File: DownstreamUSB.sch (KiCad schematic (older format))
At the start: 2 parts, among them J4 USB_A

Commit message: Replace 100 uF caps
The ones I had selected before were only rated for 4V, and I need at least 5V (USB bus).
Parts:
- C17: Manufacturer_Part_Number TPST107M004R0500 -> TACT107M006XTA; Price 0.93 -> 4.4; Vendor Part Number 581-TPST107M004R0500 -> 581-TACT107M006XTA
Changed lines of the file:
@@
 F 1 "100μF" H 5435 3055 50 0000 R CNN
 F 2 "Capacitor_SMD:C_1210_3225Metric" H 5588 2950 50 0001 C CNN
-F 3 "https://www.mouser.com/datasheet/2/40/TPS-2066671.pdf" H 5550 3100 50 0001 C CNN
+F 3 "https://www.mouser.com/datasheet/2/40/tac-776418.pdf" H 5550 3100 50 0001 C CNN
 F 4 "AVX" H 5435 3246 50 0001 C CNN "Manufacturer_Name"
-F 5 "TPST107M004R0500" H 5435 3246 50 0001 C CNN "Manufacturer_Part_Number"
-F 6 "0.93" H 5435 3246 50 0001 C CNN "Price"
-F 7 "581-TPST107M004R0500" H 5435 3246 50 0001 C CNN "Vendor Part Number"
+F 5 "TACT107M006XTA" H 5435 3246 50 0001 C CNN "Manufacturer_Part_Number"
+F 6 "4.4" H 5435 3246 50 0001 C CNN "Price"
+F 7 "581-TACT107M006XTA" H 5435 3246 50 0001 C CNN "Vendor Part Number"
 F 8 "Mouser" H 5435 3246 50 0001 C CNN "Vendor"
 	1    5550 3100

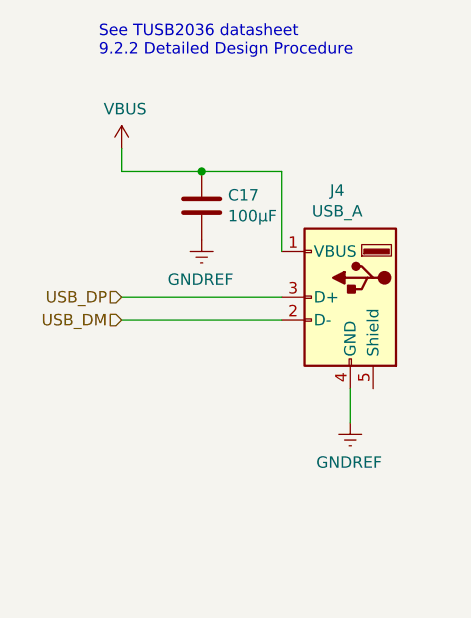
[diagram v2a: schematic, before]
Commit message: Add ID markings on schema and pcb
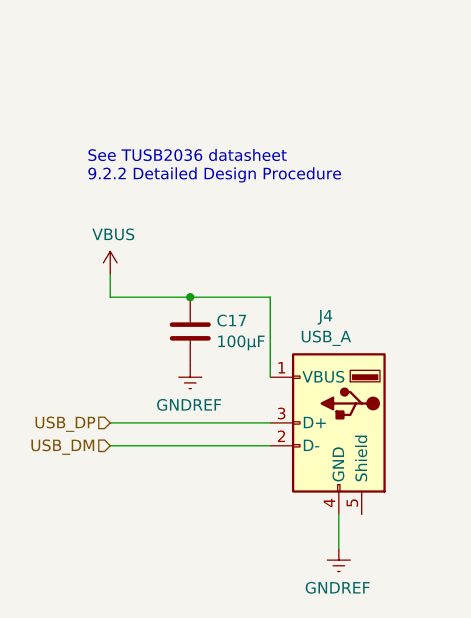
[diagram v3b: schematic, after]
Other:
- moved on the sheet: C17, J4
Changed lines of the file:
@@
 encoding utf-8
 Sheet 6 6
-Title ""
-Date ""
-Rev ""
-Comp ""
+Title "TX-500 Data Interface"
+Date "2021-03-15"
+Rev "0.1"
+Comp "Chris Keller K0SWE"
 Comment1 ""
 Comment2 ""
@@
 L power:GNDREF #PWR?
 U 1 1 6054D05F
-P 5550 3250
+P 5500 3800
 AR Path="/6057976E/6054D05F" Ref="#PWR?"  Part="1"
 AR Path="/605B3ED2/6054D05F" Ref="#PWR0134"  Part="1"
-F 0 "#PWR0134" H 5550 3000 50  0001 C CNN
-F 1 "GNDREF" H 5555 3077 50  0000 C CNN
-F 2 "" H 5550 3250 50  0001 C CNN
-F 3 "" H 5550 3250 50  0001 C CNN
-	1    5550 3250
+F 0 "#PWR0134" H 5500 3550 50  0001 C CNN
+F 1 "GNDREF" H 5505 3627 50  0000 C CNN
+F 2 "" H 5500 3800 50  0001 C CNN
+F 3 "" H 5500 3800 50  0001 C CNN
+	1    5500 3800
 	-1   0    0    -1
 $EndComp
@@
 L power:GNDREF #PWR?
 U 1 1 605EED26
-P 6200 4050
+P 6150 4600
 AR Path="/6057976E/605EED26" Ref="#PWR?"  Part="1"
 AR Path="/605B3ED2/605EED26" Ref="#PWR0116"  Part="1"
-F 0 "#PWR0116" H 6200 3800 50  0001 C CNN
-F 1 "GNDREF" H 6205 3877 50  0000 C CNN
-F 2 "" H 6200 4050 50  0001 C CNN
-F 3 "" H 6200 4050 50  0001 C CNN
-	1    6200 4050
+F 0 "#PWR0116" H 6150 4350 50  0001 C CNN
+F 1 "GNDREF" H 6155 4427 50  0000 C CNN
+F 2 "" H 6150 4600 50  0001 C CNN
+F 3 "" H 6150 4600 50  0001 C CNN
+	1    6150 4600
 	-1   0    0    -1
 $EndComp
@@
 L power:VBUS #PWR0113
 U 1 1 605E55CB
-P 5200 2850
-F 0 "#PWR0113" H 5200 2700 50  0001 C CNN
-F 1 "VBUS" H 5215 3023 50  0000 C CNN
-F 2 "" H 5200 2850 50  0001 C CNN
-F 3 "" H 5200 2850 50  0001 C CNN
-	1    5200 2850
+P 5150 3400
+F 0 "#PWR0113" H 5150 3250 50  0001 C CNN
+F 1 "VBUS" H 5165 3573 50  0000 C CNN
+F 2 "" H 5150 3400 50  0001 C CNN
+F 3 "" H 5150 3400 50  0001 C CNN
+	1    5150 3400
 	1    0    0    -1
 $EndComp
@@
 L Connector:USB_A J?
 U 1 1 605B68EE
-P 6200 3500
+P 6150 4050
 AR Path="/605B68EE" Ref="J?"  Part="1"
 AR Path="/605B3ED2/605B68EE" Ref="J4"  Part="1"
-F 0 "J4" H 6257 3967 50  0000 C CNN
-F 1 "USB_A" H 6257 3876 50  0000 C CNN
-F 2 "Connector_USB:USB_A_Molex_67643_Horizontal" H 6350 3450 50  0001 C CNN
-F 3 "https://www.mouser.com/datasheet/2/276/1/0676433910_IO_CONNECTORS-172273.pdf" H 6350 3450 50  0001 C CNN
-F 4 "Downstream USB socket" H 6257 4067 50  0001 C CNN "Description"
-F 5 "Molex" H 6257 4067 50  0001 C CNN "Manufacturer_Name"
-F 6 "67643-3910" H 6257 4067 50  0001 C CNN "Manufacturer_Part_Number"
-F 7 "1.64" H 6257 4067 50  0001 C CNN "Price"
-F 8 "538-67643-3910" H 6257 4067 50  0001 C CNN "Vendor Part Number"
-F 9 "Mouser" H 6257 4067 50  0001 C CNN "Vendor"
-	1    6200 3500
+F 0 "J4" H 6207 4517 50  0000 C CNN
+F 1 "USB_A" H 6207 4426 50  0000 C CNN
+F 2 "Connector_USB:USB_A_Molex_67643_Horizontal" H 6300 4000 50  0001 C CNN
+F 3 "https://www.mouser.com/datasheet/2/276/1/0676433910_IO_CONNECTORS-172273.pdf" H 6300 4000 50  0001 C CNN
+F 4 "Downstream USB socket" H 6207 4617 50  0001 C CNN "Description"
+F 5 "Molex" H 6207 4617 50  0001 C CNN "Manufacturer_Name"
+F 6 "67643-3910" H 6207 4617 50  0001 C CNN "Manufacturer_Part_Number"
+F 7 "1.64" H 6207 4617 50  0001 C CNN "Price"
+F 8 "538-67643-3910" H 6207 4617 50  0001 C CNN "Vendor Part Number"
+F 9 "Mouser" H 6207 4617 50  0001 C CNN "Vendor"
+	1    6150 4050
 	-1   0    0    -1
 $EndComp
@@
 L Device:C C?
 U 1 1 605EE4F2
-P 5550 3100
+P 5500 3650
 AR Path="/605EE4F2" Ref="C?"  Part="1"
 AR Path="/6057976E/605EE4F2" Ref="C?"  Part="1"
 AR Path="/605B3ED2/605EE4F2" Ref="C17"  Part="1"
-F 0 "C17" H 5435 3146 50  0000 R CNN
-F 1 "100μF" H 5435 3055 50  0000 R CNN
-F 2 "Capacitor_SMD:C_1210_3225Metric" H 5588 2950 50  0001 C CNN
-F 3 "https://www.mouser.com/datasheet/2/40/tac-776418.pdf" H 5550 3100 50  0001 C CNN
-F 4 "AVX" H 5435 3246 50  0001 C CNN "Manufacturer_Name"
-F 5 "TACT107M006XTA" H 5435 3246 50  0001 C CNN "Manufacturer_Part_Number"
-F 6 "4.4" H 5435 3246 50  0001 C CNN "Price"
-F 7 "581-TACT107M006XTA" H 5435 3246 50  0001 C CNN "Vendor Part Number"
-F 8 "Mouser" H 5435 3246 50  0001 C CNN "Vendor"
-	1    5550 3100
+F 0 "C17" H 5385 3696 50  0000 R CNN
+F 1 "100μF" H 5385 3605 50  0000 R CNN
+F 2 "Capacitor_SMD:C_1210_3225Metric" H 5538 3500 50  0001 C CNN
+F 3 "https://www.mouser.com/datasheet/2/40/tac-776418.pdf" H 5500 3650 50  0001 C CNN
+F 4 "AVX" H 5385 3796 50  0001 C CNN "Manufacturer_Name"
+F 5 "TACT107M006XTA" H 5385 3796 50  0001 C CNN "Manufacturer_Part_Number"
+F 6 "4.4" H 5385 3796 50  0001 C CNN "Price"
+F 7 "581-TACT107M006XTA" H 5385 3796 50  0001 C CNN "Vendor Part Number"
+F 8 "Mouser" H 5385 3796 50  0001 C CNN "Vendor"
+	1    5500 3650
 	-1   0    0    -1
 $EndComp
-Text Notes 5100 2450 0    50   ~ 0
+Text Notes 5050 3000 0    50   ~ 0
 See TUSB2036 datasheet\n9.2.2 Detailed Design Procedure
-Text HLabel 5200 3500 0    50   Input ~ 0
+Text HLabel 5150 4050 0    50   Input ~ 0
 USB_DP
-Text HLabel 5200 3600 0    50   Input ~ 0
+Text HLabel 5150 4150 0    50   Input ~ 0
 USB_DM
 Wire Wire Line
-	6200 4050 6200 3900
+	6150 4600 6150 4450
 Wire Wire Line
-	5900 2950 5900 3300
+	5850 3500 5850 3850
 Wire Wire Line
-	5200 2850 5200 2950
+	5150 3400 5150 3500
 Wire Wire Line
-	5550 2950 5900 2950
+	5500 3500 5850 3500
 Wire Wire Line
-	5200 2950 5550 2950
+	5150 3500 5500 3500
 Wire Wire Line
-	5200 3500 5900 3500
+	5150 4050 5850 4050
 Wire Wire Line
-	5200 3600 5900 3600
-Connection ~ 5550 2950
+	5150 4150 5850 4150
+Connection ~ 5500 3500
 $EndSCHEMATC

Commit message: First pass at routing PCB
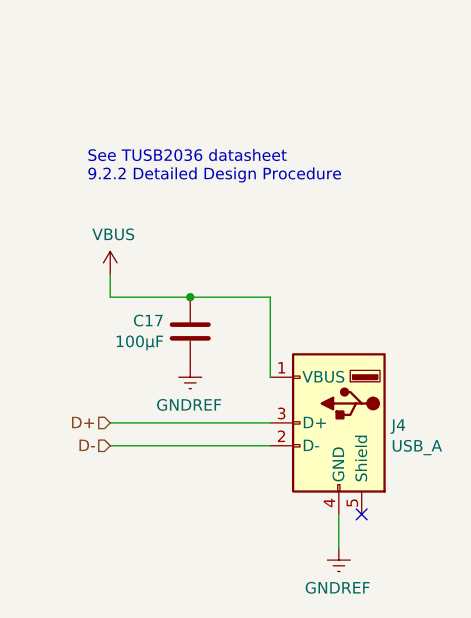
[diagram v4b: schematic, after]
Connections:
- net USB_DM renamed D-
- net USB_DP renamed D+
- no-connect marks 0 -> 1
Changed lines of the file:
@@
 Rev "0.1"
 Comp "Chris Keller K0SWE"
-Comment1 ""
+Comment1 "Licensed under Apache-2.0"
 Comment2 ""
 Comment3 ""
@@
 AR Path="/605B68EE" Ref="J?"  Part="1"
 AR Path="/605B3ED2/605B68EE" Ref="J4"  Part="1"
-F 0 "J4" H 6207 4517 50  0000 C CNN
-F 1 "USB_A" H 6207 4426 50  0000 C CNN
+F 0 "J4" H 5920 4039 50  0000 R CNN
+F 1 "USB_A" H 5920 3948 50  0000 R CNN
 F 2 "Connector_USB:USB_A_Molex_67643_Horizontal" H 6300 4000 50  0001 C CNN
 F 3 "https://www.mouser.com/datasheet/2/276/1/0676433910_IO_CONNECTORS-172273.pdf" H 6300 4000 50  0001 C CNN
@@
 AR Path="/6057976E/605EE4F2" Ref="C?"  Part="1"
 AR Path="/605B3ED2/605EE4F2" Ref="C17"  Part="1"
-F 0 "C17" H 5385 3696 50  0000 R CNN
-F 1 "100μF" H 5385 3605 50  0000 R CNN
+F 0 "C17" H 5615 3696 50  0000 L CNN
+F 1 "100μF" H 5615 3605 50  0000 L CNN
 F 2 "Capacitor_SMD:C_1210_3225Metric" H 5538 3500 50  0001 C CNN
 F 3 "https://www.mouser.com/datasheet/2/40/tac-776418.pdf" H 5500 3650 50  0001 C CNN
@@
 See TUSB2036 datasheet\n9.2.2 Detailed Design Procedure
 Text HLabel 5150 4050 0    50   Input ~ 0
-USB_DP
+D+
 Text HLabel 5150 4150 0    50   Input ~ 0
-USB_DM
+D-
 Wire Wire Line
 	6150 4600 6150 4450
@@
 	5150 4150 5850 4150
 Connection ~ 5500 3500
+NoConn ~ 6250 4450
 $EndSCHEMATC

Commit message: Replace USB-A port with SMD
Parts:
- J4: footprint Connector_USB:USB_A_Molex_67643_Horizontal -> Wurth-USBA:62900416021; Manufacturer_Name Molex -> Wurth; Manufacturer_Part_Number 67643-3910 -> 62900416021; Price 1.64 -> 2.36; Vendor Part Number 538-67643-3910 -> 710-62900416021
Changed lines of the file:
@@
-$EndComp
-$Comp
-L Connector:USB_A J?
-U 1 1 605B68EE
-P 6150 4050
-AR Path="/605B68EE" Ref="J?"  Part="1"
-AR Path="/605B3ED2/605B68EE" Ref="J4"  Part="1"
-F 0 "J4" H 5920 4039 50  0000 R CNN
-F 1 "USB_A" H 5920 3948 50  0000 R CNN
-F 2 "Connector_USB:USB_A_Molex_67643_Horizontal" H 6300 4000 50  0001 C CNN
-F 3 "https://www.mouser.com/datasheet/2/276/1/0676433910_IO_CONNECTORS-172273.pdf" H 6300 4000 50  0001 C CNN
-F 4 "Downstream USB socket" H 6207 4617 50  0001 C CNN "Description"
-F 5 "Molex" H 6207 4617 50  0001 C CNN "Manufacturer_Name"
-F 6 "67643-3910" H 6207 4617 50  0001 C CNN "Manufacturer_Part_Number"
-F 7 "1.64" H 6207 4617 50  0001 C CNN "Price"
-F 8 "538-67643-3910" H 6207 4617 50  0001 C CNN "Vendor Part Number"
-F 9 "Mouser" H 6207 4617 50  0001 C CNN "Vendor"
-	1    6150 4050
-	-1   0    0    -1
 $EndComp
 $Comp
@@
 Connection ~ 5500 3500
 NoConn ~ 6250 4450
+$Comp
+L Connector:USB_A J?
+U 1 1 605B68EE
+P 6150 4050
+AR Path="/605B68EE" Ref="J?"  Part="1"
+AR Path="/605B3ED2/605B68EE" Ref="J4"  Part="1"
+F 0 "J4" H 5920 4039 50  0000 R CNN
+F 1 "USB_A" H 5920 3948 50  0000 R CNN
+F 2 "Wurth-USBA:62900416021" H 6300 4000 50  0001 C CNN
+F 3 "https://www.mouser.com/datasheet/2/445/62900416021-1718169.pdf" H 6300 4000 50  0001 C CNN
+F 4 "Downstream USB socket" H 6207 4617 50  0001 C CNN "Description"
+F 5 "Wurth" H 6207 4617 50  0001 C CNN "Manufacturer_Name"
+F 6 "62900416021" H 6207 4617 50  0001 C CNN "Manufacturer_Part_Number"
+F 7 "2.36" H 6207 4617 50  0001 C CNN "Price"
+F 8 "710-62900416021" H 6207 4617 50  0001 C CNN "Vendor Part Number"
+F 9 "Mouser" H 6207 4617 50  0001 C CNN "Vendor"
+	1    6150 4050
+	-1   0    0    -1
+$EndComp
 $EndSCHEMATC
